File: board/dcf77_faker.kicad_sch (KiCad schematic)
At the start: 46 parts, among them J1 Barrel_Jack, J2 DBG, J3 ANT, J4 LCD_I2C, SW1 RST, SW2 H, SW3 MIN, SW4 S, U1 NCP1117ST33T3G, U2 ATSAML21G18B-AUT, X1 32.768kHz, X2 31MHz

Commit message: board: fix button LCSC number
we still had the flat ones
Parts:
- J2: LCSC C9900020485 -> C5250218
- SW1, SW2, SW3, SW4: LCSC C2834943 -> C393942
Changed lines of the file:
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@@
       (effects (font (size 1.27 1.27)) hide)
     )
-    (property "LCSC" "C2834943" (id 4) (at 78.74 180.34 0)
+    (property "LCSC" "C393942" (id 4) (at 78.74 180.34 0)
       (effects (font (size 1.27 1.27)) hide)
     )
@@
       (effects (font (size 1.27 1.27)) hide)
     )
-    (property "LCSC" "C2834943" (id 4) (at 274.32 148.59 0)
+    (property "LCSC" "C393942" (id 4) (at 274.32 148.59 0)
       (effects (font (size 1.27 1.27)) hide)
     )
@@
       (effects (font (size 1.27 1.27)) hide)
     )
-    (property "LCSC" "C9900020485" (id 4) (at 247.65 83.82 0)
+    (property "LCSC" "C5250218" (id 4) (at 247.65 83.82 0)
       (effects (font (size 1.27 1.27)) hide)
     )
@@
       (effects (font (size 1.27 1.27)) hide)
     )
-    (property "LCSC" "C2834943" (id 4) (at 78.74 190.5 0)
+    (property "LCSC" "C393942" (id 4) (at 78.74 190.5 0)
       (effects (font (size 1.27 1.27)) hide)
     )
@@
       (effects (font (size 1.27 1.27)) hide)
     )
-    (property "LCSC" "C2834943" (id 4) (at 78.74 170.18 0)
-      (effects (font (size 1.27 1.27)) hide)
-    )
+    (property "LCSC" "C393942" (id 4) (at 78.74 170.18 0)
+      (effects (font (size 1.27 1.27)) hide)
+    )

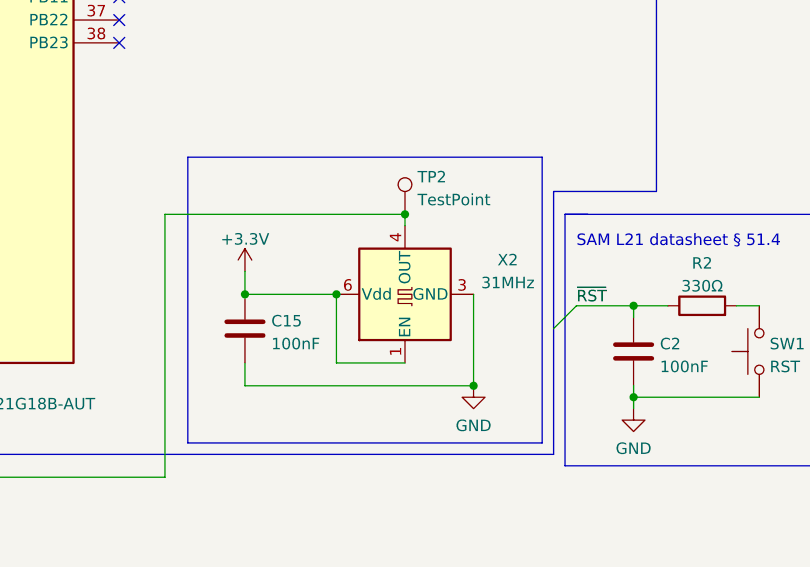
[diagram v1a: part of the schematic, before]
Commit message: board: replace X2 with 7x5mm footprint (Microchip DSC8001A)
this should make it easier to hand-solder after programming
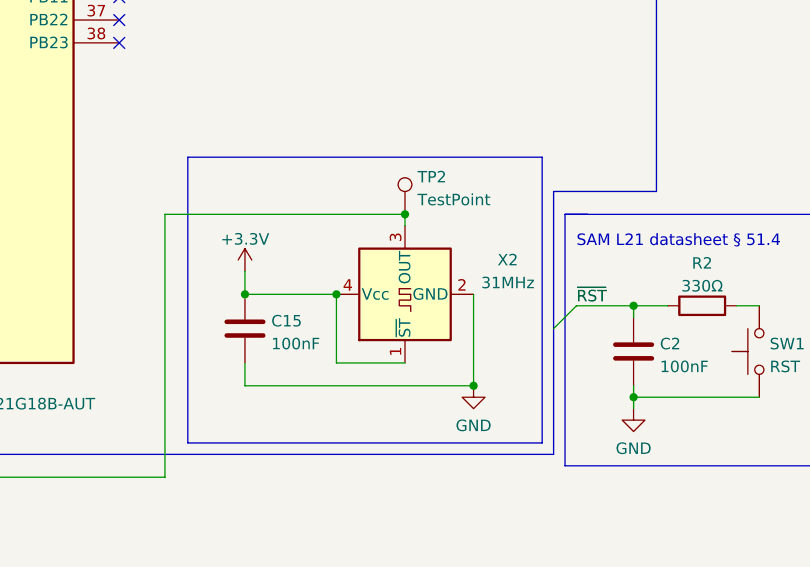
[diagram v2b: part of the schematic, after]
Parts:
- X2: footprint Oscillator_Microchip:Oscillator_SMD_Microchip_DSC1101D-6Pin_2.5x2.0mm -> Oscillator_Microchip:Oscillator_SMD_Microchip_DSC8001A-6Pin_7.0x5.0mm; symbol Oscillator_Microchip:DSC1101D -> Oscillator:SG-210STF; LCSC C390485 -> (none); Manufacturer Seiko Epson -> Microchip; Model SG-8018CE 20.000000MHz TJHPA -> DSC8001A
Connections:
- net +3.3V: now also X2.4 (Vcc); no longer X2.6 (Vdd)
- net GND: now also X2.2 (GND); no longer X2.3 (GND)
- net XIN: now also X2.3 (OUT); no longer X2.4 (OUT)
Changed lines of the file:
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@@
     (pin "2")
   )
-  (symbol (lib_id "Oscillator_Microchip:DSC1101D") (at 234.95 142.24 90) (unit 1)
+  (symbol (lib_id "Oscillator:SG-210STF") (at 234.95 142.24 90) (unit 1)
     (in_bom yes) (on_board yes)
     (property "Reference" "X2" (id 0) (at 246.38 138.43 90))
     (property "Value" "31MHz" (id 1) (at 246.38 140.97 90))
-    (property "Footprint" "Oscillator_Microchip:Oscillator_SMD_Microchip_DSC1101D-6Pin_2.5x2.0mm" (id 2) (at 243.84 124.46 0)
-      (effects (font (size 1.27 1.27)) hide)
-    )
-    (property "Datasheet" "https://ww1.microchip.com/downloads/en/DeviceDoc/DSC1101-21-Low-Jitter-Precision-CMOS-Oscillator-DS20005613D.pdf" (id 3) (at 234.95 144.78 0)
-      (effects (font (size 1.27 1.27)) hide)
-    )
-    (property "Manufacturer" "Seiko Epson" (id 4) (at 234.95 142.24 0)
-      (effects (font (size 1.27 1.27)) hide)
-    )
-    (property "Model" "SG-8018CE 20.000000MHz TJHPA" (id 5) (at 234.95 142.24 0)
-      (effects (font (size 1.27 1.27)) hide)
-    )
-    (property "LCSC" "C390485" (id 6) (at 234.95 142.24 0)
+    (property "Footprint" "Oscillator_Microchip:Oscillator_SMD_Microchip_DSC8001A-6Pin_7.0x5.0mm" (id 2) (at 243.84 130.81 0)
+      (effects (font (size 1.27 1.27)) hide)
+    )
+    (property "Datasheet" "https://ww1.microchip.com/downloads/en/DeviceDoc/DSC8001%20Datasheet%20MKQBPD09011003-2.pdf" (id 3) (at 234.95 144.78 0)
+      (effects (font (size 1.27 1.27)) hide)
+    )
+    (property "Manufacturer" "Microchip" (id 4) (at 234.95 142.24 0)
+      (effects (font (size 1.27 1.27)) hide)
+    )
+    (property "Model" "DSC8001A" (id 5) (at 234.95 142.24 0)
+      (effects (font (size 1.27 1.27)) hide)
+    )
+    (property "LCSC" "" (id 6) (at 234.95 142.24 0)
       (effects (font (size 1.27 1.27)) hide)
     )
@@
     (pin "3")
     (pin "4")
-    (pin "5")
-    (pin "6")
   )
   (symbol (lib_id "Device:C_Polarized") (at 17.78 57.15 0) (unit 1)
@@
     )
     (path "/d0cd7e50-71db-44f5-a7de-bdbe89fb0723"
-      (reference "X2") (unit 1) (value "31MHz") (footprint "Oscillator_Microchip:Oscillator_SMD_Microchip_DSC1101D-6Pin_2.5x2.0mm")
-    )
-  )
+      (reference "X2") (unit 1) (value "31MHz") (footprint "Oscillator_Microchip:Oscillator_SMD_Microchip_DSC8001A-6Pin_7.0x5.0mm")
+    )
+  )
